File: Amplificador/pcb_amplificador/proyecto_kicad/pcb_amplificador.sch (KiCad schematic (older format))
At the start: 139 parts, among them CON1 SJ-3523-SMT-TR, J1 Screw_Terminal_01x02, J2 Screw_Terminal_01x02, J3 Screw_Terminal_01x02, J4 Screw_Terminal_01x02, J5 Conn_01x03_Male, J6 Screw_Terminal_01x02, J7 Screw_Terminal_01x02, K1 FINDER-40.11-2016, M1 FDS9934C, M2 FDS9934C, Q1 BC860, Q10 BD139, Q11 BD140, Q12 BD139, Q13 2SA1943-O_Q_, Q14 2SC5200-O_Q, Q15 2SA1943-O_Q_, Q16 2SC5200-O_Q, Q17 2SAR514P5, Q18 BC860, Q19 BC860, Q2 BC860, Q20 2SAR514P5, Q21 2SCR514P5, Q22 2SCR514P5, Q23 2SCR514P5, Q24 2SAR514P5, Q25 2SCR514P5, Q26 BC817, Q27 BC817, Q28 BC807, Q29 BS170, Q3 BC850, Q4 BC850, Q5 BC860, Q6 BC860, Q7 BC850, Q8 2SCR514P5, Q9 2SCR514P5

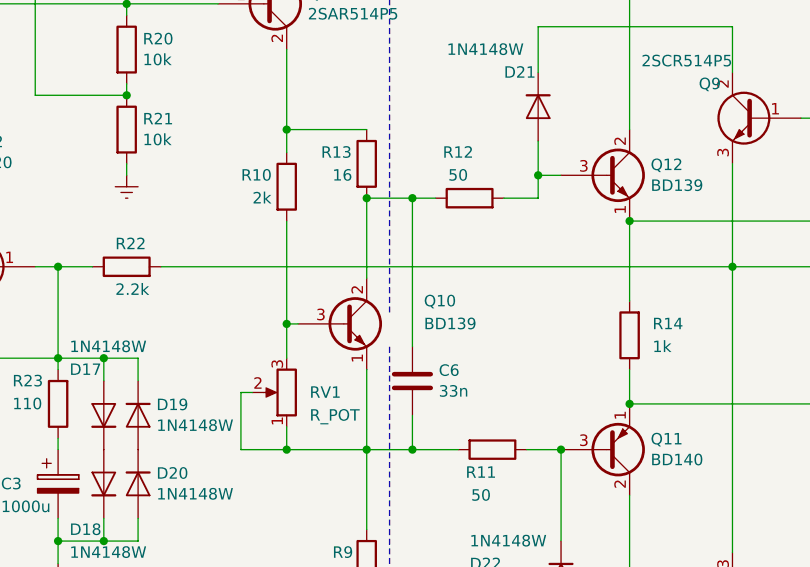
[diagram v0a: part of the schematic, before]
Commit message: Cambios varios en la documentación del amplificador; agregado de ecuaciones en latex y gráficos al archivo que explica como se hallaron los valores de los componentes; agregado de documento que explica paso a paso el funcionamiento de los conmutadores de salida
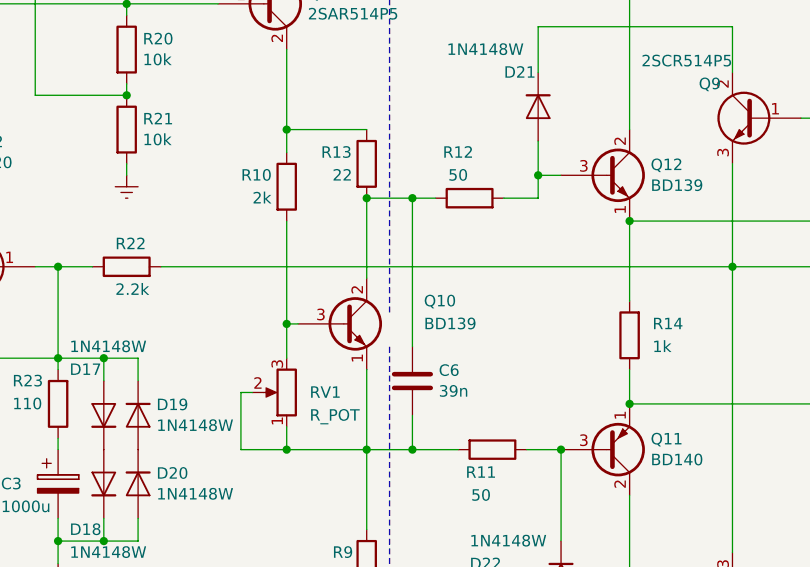
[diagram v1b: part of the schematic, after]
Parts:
- C6: value 33n -> 39n
- R13: value 16 -> 22
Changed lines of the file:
@@
 EESchema Schematic File Version 4
 LIBS:pcb_amplificador-cache
-EELAYER 26 0
+EELAYER 29 0
 EELAYER END
 $Descr A4 11693 8268
@@
 P 4150 2700
 F 0 "R13" H 3950 2750 50  0000 L CNN
-F 1 "16" H 4000 2650 50  0000 L CNN
+F 1 "22" H 4000 2650 50  0000 L CNN
 F 2 "Resistor_SMD:R_0805_2012Metric_Pad1.15x1.40mm_HandSolder" V 4080 2700 50  0001 C CNN
 F 3 "~" H 4150 2700 50  0001 C CNN
@@
 P 4350 3650
 F 0 "C6" H 4235 3604 50  0000 R CNN
-F 1 "33n" H 4235 3695 50  0000 R CNN
+F 1 "39n" H 4235 3695 50  0000 R CNN
 F 2 "Capacitor_SMD:C_0805_2012Metric_Pad1.15x1.40mm_HandSolder" H 4388 3500 50  0001 C CNN
 F 3 "~" H 4350 3650 50  0001 C CNN

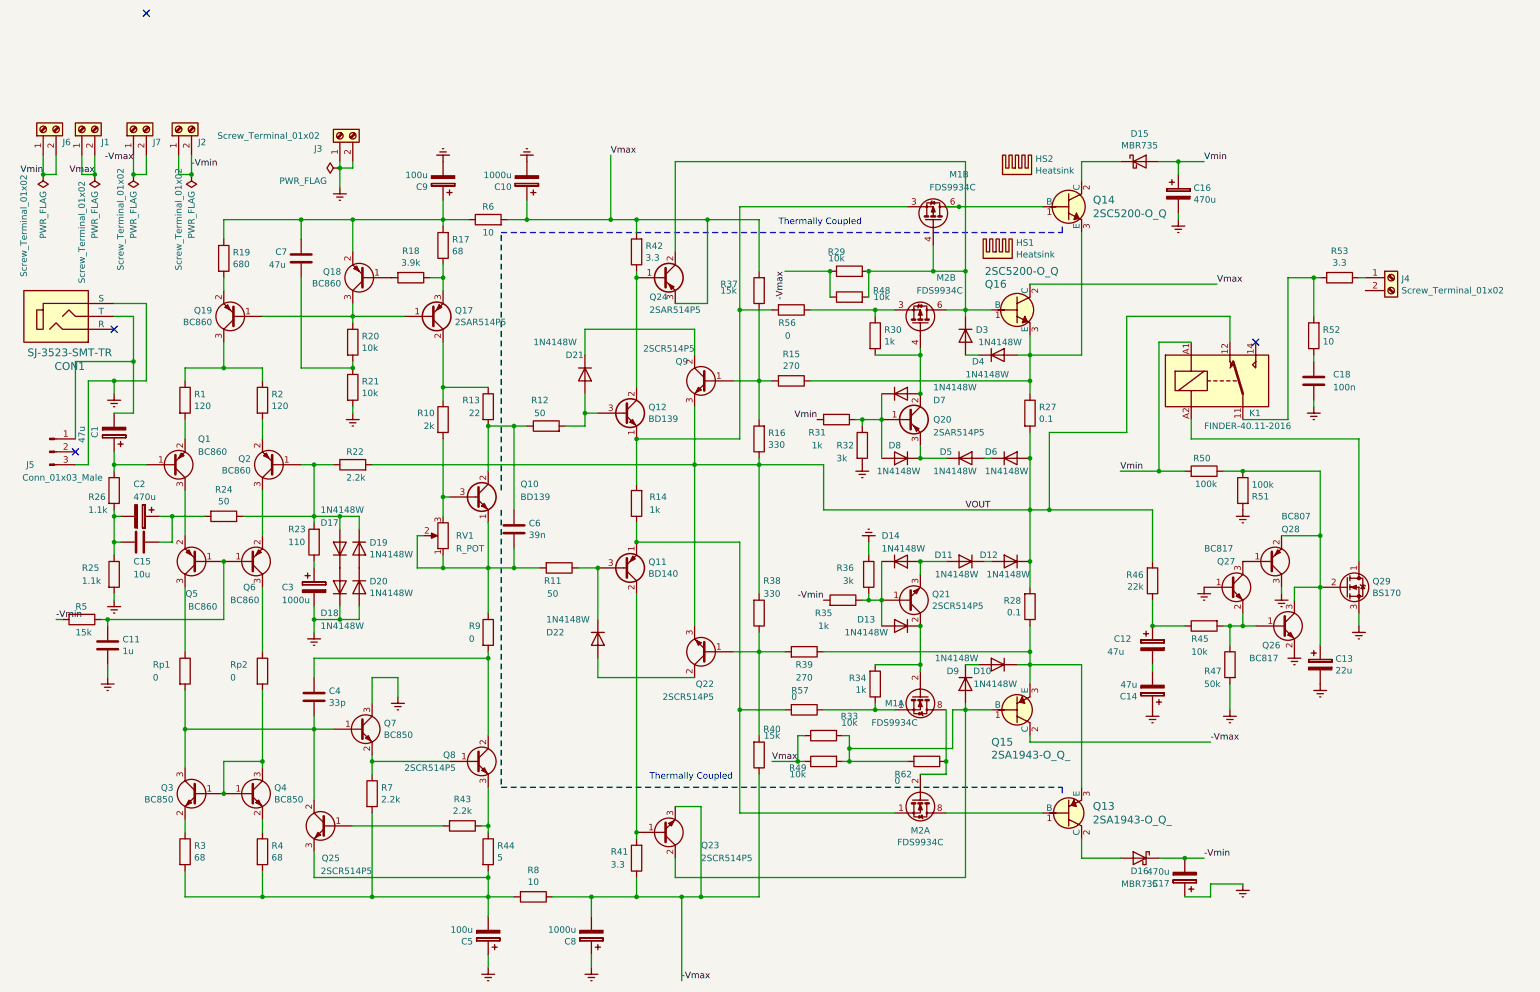
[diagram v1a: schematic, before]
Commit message: Agregado de datos extra de los componentes en el esquemático del amplificador y cambios menores
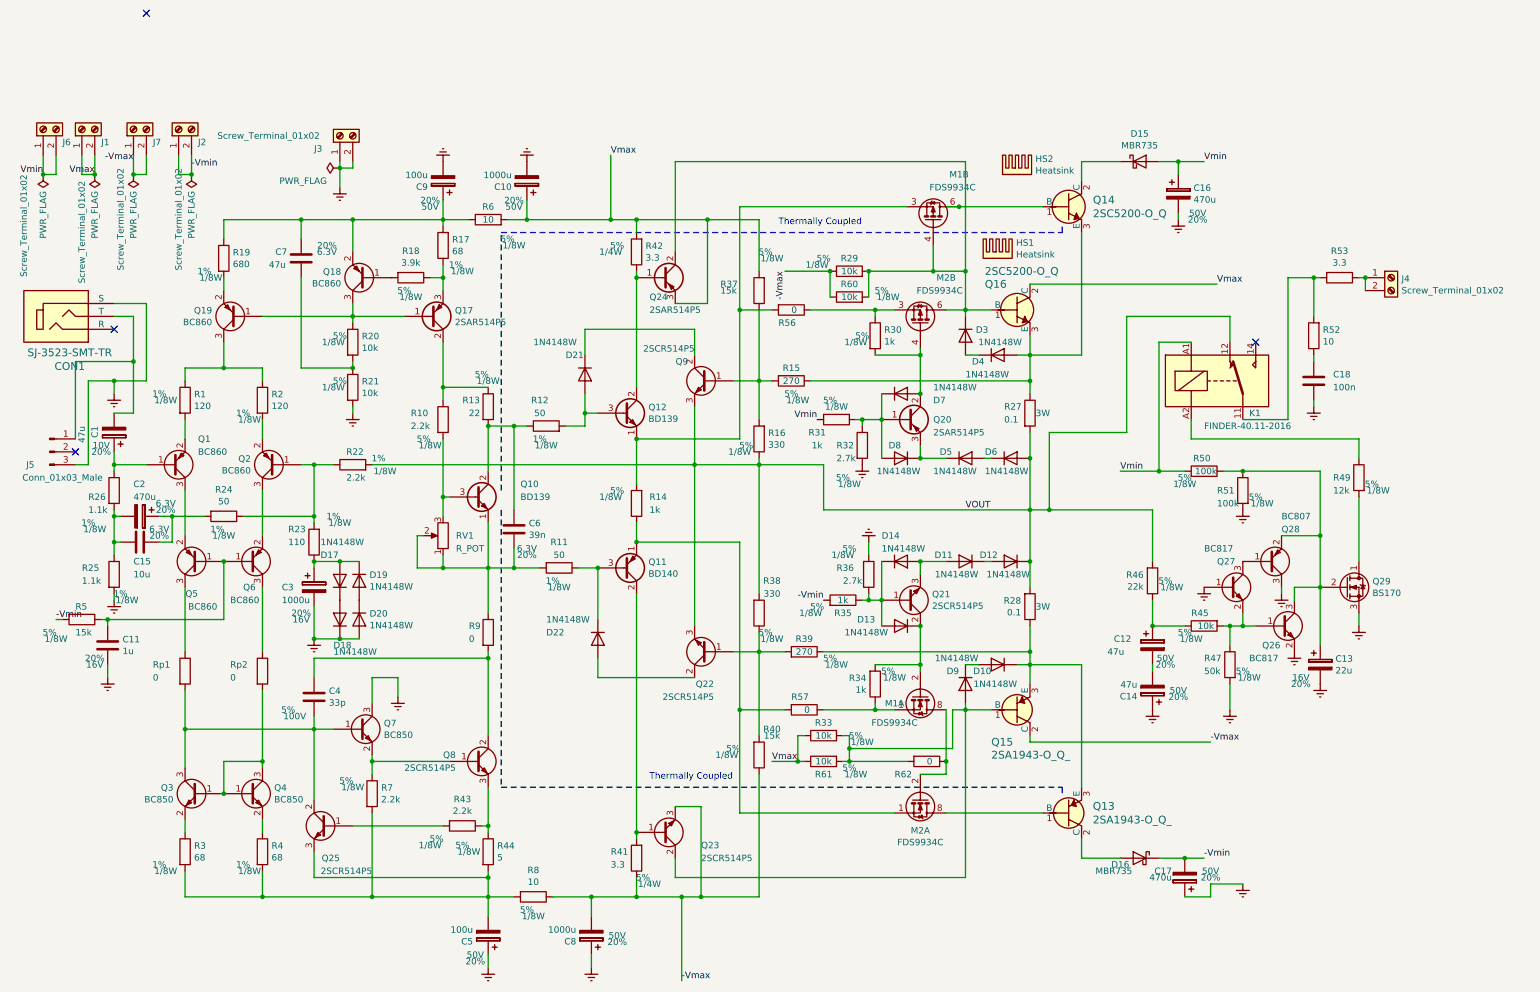
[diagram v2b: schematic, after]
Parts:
- added R49: 12k, Resistor_SMD:R_0805_2012Metric_Pad1.15x1.40mm_HandSolder, symbol Device:R
- C1: Tolerance (none) -> 20%; Voltage (none) -> 10V
- C10, C12, C14, C16, C17, C5, C8, C9: Tolerance (none) -> 20%; Voltage (none) -> 50V
- C11, C13, C3: Tolerance (none) -> 20%; Voltage (none) -> 16V
- C15, C2, C6, C7: Tolerance (none) -> 20%; Voltage (none) -> 6.3V
- C4: Tolerance (none) -> 5%; Voltage (none) -> 100V
- R1, R11, R12, R17, R19, R2, R22, R23, R24, R25, R26, R3, R4: Power (none) -> 1/8W; Tolerance (none) -> 1%
- R10: value 2k -> 2.2k; Power (none) -> 1/8W; Tolerance (none) -> 5%
- R13, R14, R15, R16, R18, R20, R21, R29, R30, R31, R33, R34, R35, R37, R38, R39, R40, R43, R44, R45, R46, R47, R5, R50, R51, R6, R7, R8: Power (none) -> 1/8W; Tolerance (none) -> 5%
- R27, R28: Power (none) -> 3W
- R32, R36: value 3k -> 2.7k; Power (none) -> 1/8W; Tolerance (none) -> 5%
- R41, R42: Power (none) -> 1/4W; Tolerance (none) -> 5%
- R60: renamed from R48; Power (none) -> 1/8W; Tolerance (none) -> 5%
- R61: renamed from R49; Power (none) -> 1/8W; Tolerance (none) -> 5%
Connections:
- net at Q2.1 (B), R22.1, R23.2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: no longer D17.2 (A), D19.1 (K)
- net at C3.1, R23.1: now also D17.2 (A), D19.1 (K)
- net at J4.1 (Pin_1), R53.1: now also J4.2 (Pin_2)
- net at Q29.1 (D): now also R49.2; no longer K1.A2
- new net: K1.A2, R49.1
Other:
- moved on the sheet: D17, D18, D19, D20

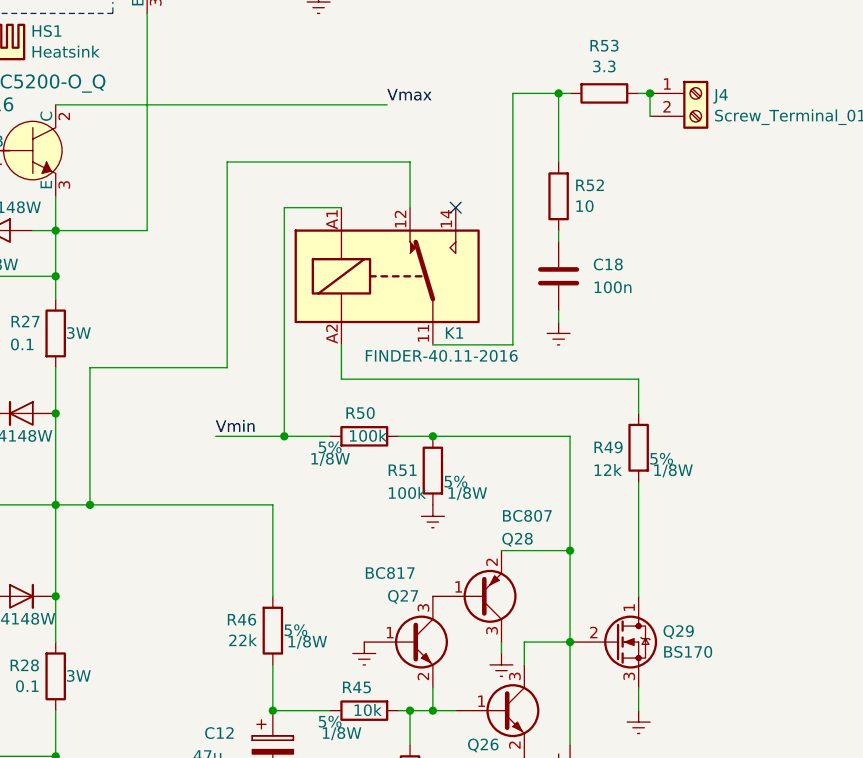
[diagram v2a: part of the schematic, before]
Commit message: Agregado de los resultados de la medicion de la proteccion de DC
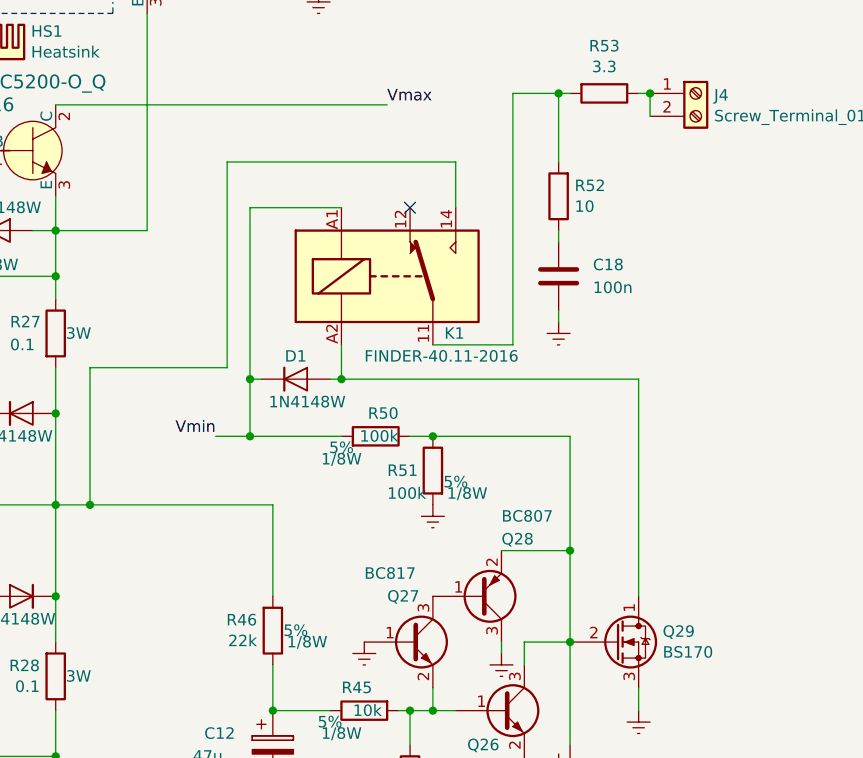
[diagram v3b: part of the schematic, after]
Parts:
- removed R49: 12k, Resistor_SMD:R_0805_2012Metric_Pad1.15x1.40mm_HandSolder, symbol Device:R
- added D1: 1N4148W, Diode_SMD:D_SOD-123, symbol Diode:1N4148W
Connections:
- net VOUT: now also K1.14; no longer K1.12
- net Vmin: now also D1.1 (K)
- net at Q29.1 (D): now also K1.A2, D1.2 (A)
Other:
- moved on the sheet: R50
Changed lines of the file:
@@
 EESchema Schematic File Version 4
 LIBS:pcb_amplificador-cache
-EELAYER 26 0
+EELAYER 29 0
 EELAYER END
 $Descr A4 11693 8268
@@
 L Device:R R50
 U 1 1 5D0A4886
-P 9700 3200
-F 0 "R50" V 9800 3250 50  0000 R CNN
-F 1 "100k" V 9700 3300 50  0000 R CNN
-F 2 "Resistor_SMD:R_0805_2012Metric_Pad1.15x1.40mm_HandSolder" V 9630 3200 50  0001 C CNN
-F 3 "~" H 9700 3200 50  0001 C CNN
-F 4 "5%" V 9650 3050 50  0000 C CNN "Tolerance"
-F 5 "1/8W" V 9600 3050 50  0000 C CNN "Power"
-	1    9700 3200
+P 9750 3200
+F 0 "R50" V 9850 3300 50  0000 R CNN
+F 1 "100k" V 9750 3300 50  0000 R CNN
+F 2 "Resistor_SMD:R_0805_2012Metric_Pad1.15x1.40mm_HandSolder" V 9680 3200 50  0001 C CNN
+F 3 "~" H 9750 3200 50  0001 C CNN
+F 4 "5%" V 9700 3050 50  0000 C CNN "Tolerance"
+F 5 "1/8W" V 9650 3050 50  0000 C CNN "Power"
+	1    9750 3200
 	0    1    -1   0
 $EndComp
@@
 $EndComp
 Wire Wire Line
-	9850 3200 10000 3200
+	9900 3200 10000 3200
 Wire Wire Line
 	10600 3200 10600 3700
@@
 	10600 4100 10600 4550
 Wire Wire Line
-	10900 3900 10900 3400
-Wire Wire Line
-	9350 3200 9350 2200
-Wire Wire Line
 	9100 2000 9100 2900
 Wire Wire Line
@@
 Wire Wire Line
 	10600 3700 10600 4100
-Wire Wire Line
-	9350 3200 9550 3200
 Wire Wire Line
 	10000 3200 10600 3200
@@
 Text Label 9750 5300 0    50   ~ 0
 -Vmax
-Text Label 9050 3200 0    50   ~ 0
+Text Label 9050 3200 2    50   ~ 0
 Vmin
 Text Label 9800 1750 0    50   ~ 0
@@
 Wire Wire Line
 	4150 4650 4150 5250
-Wire Wire Line
-	9350 2200 9600 2200
 Text Label 7850 3500 0    50   ~ 0
 VOUT
@@
 Text Label 6750 4200 2    50   ~ 0
 -Vmin
-Connection ~ 9350 3200
 Connection ~ 6800 1650
 $Comp
@@
 	-1   0    0    1
 $EndComp
-Wire Wire Line
-	9050 3200 9350 3200
-Wire Wire Line
-	9900 2200 9900 2000
-Wire Wire Line
-	9900 2000 9100 2000
-NoConn ~ 10100 2200
 $Comp
 L Transistor_BJT:BD139 Q10
@@
 	1750 900  1850 900
 Connection ~ 1850 900
-$Comp
-L Relay:FINDER-40.11-2016 K1
-U 1 1 5DA9AF8C
-P 9800 2500
-F 0 "K1" H 10050 2250 50  0000 L CNN
-F 1 "FINDER-40.11-2016" H 9700 2150 50  0000 L CNN
-F 2 "Relay_THT:Relay_SPDT_Schrack-RP-II-1-16A-FormC_RM5mm" H 10940 2460 50  0001 C CNN
-F 3 "https://www.finder-relais.net/de/finder-relais-serie-40.pdf" H 9800 2500 50  0001 C CNN
-	1    9800 2500
-	1    0    0    -1
-$EndComp
-Wire Wire Line
-	9600 2950 9600 2800
 Wire Wire Line
 	9600 2950 10900 2950
@@
 Connection ~ 10950 1700
 Connection ~ 4150 2850
-$Comp
-L Device:R R49
-U 1 1 5D7228B4
-P 10900 3250
-F 0 "R49" H 11100 3250 50  0000 R CNN
-F 1 "12k" H 11100 3150 50  0000 R CNN
-F 2 "Resistor_SMD:R_0805_2012Metric_Pad1.15x1.40mm_HandSolder" V 10830 3250 50  0001 C CNN
-F 3 "~" H 10900 3250 50  0001 C CNN
-F 4 "5%" H 10800 3200 50  0000 C CNN "Tolerance"
-F 5 "1/8W" H 10750 3150 50  0000 C CNN "Power"
-	1    10900 3250
-	-1   0    0    -1
-$EndComp
-Wire Wire Line
-	10900 3100 10900 2950
+Wire Wire Line
+	10900 2950 10900 3900
+$Comp
+L Diode:1N4148W D1
+U 1 1 5D6AF4C4
+P 9400 2950
+F 0 "D1" H 9400 3050 50  0000 C CNN
+F 1 "1N4148W" H 9450 2850 50  0000 C CNN
+F 2 "Diode_SMD:D_SOD-123" H 9400 2775 50  0001 C CNN
+F 3 "https://www.vishay.com/docs/85748/1n4148w.pdf" H 9400 2950 50  0001 C CNN
+	1    9400 2950
+	1    0    0    -1
+$EndComp
+Wire Wire Line
+	9600 2800 9600 2950
+Connection ~ 9600 2950
+Wire Wire Line
+	9050 3200 9200 3200
+Wire Wire Line
+	9600 2950 9550 2950
+Wire Wire Line
+	9250 2950 9200 2950
+Wire Wire Line
+	9200 2950 9200 3200
+Connection ~ 9200 3200
+Wire Wire Line
+	9200 3200 9600 3200
+Wire Wire Line
+	9200 2950 9200 2200
+Wire Wire Line
+	9200 2200 9600 2200
+Connection ~ 9200 2950
+$Comp
+L Relay:FINDER-40.11-2016 K1
+U 1 1 5DA9AF8C
+P 9800 2500
+F 0 "K1" H 10050 2250 50  0000 L CNN
+F 1 "FINDER-40.11-2016" H 9700 2150 50  0000 L CNN
+F 2 "Relay_THT:Relay_SPDT_Schrack-RP-II-1-16A-FormC_RM5mm" H 10940 2460 50  0001 C CNN
+F 3 "https://www.finder-relais.net/de/finder-relais-serie-40.pdf" H 9800 2500 50  0001 C CNN
+	1    9800 2500
+	1    0    0    -1
+$EndComp
+Wire Wire Line
+	10100 2000 10100 2200
+Wire Wire Line
+	9100 2000 10100 2000
+NoConn ~ 9900 2200
 $EndSCHEMATC

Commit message: Agregado de los resultados de las mediciones de THD con las protecciones y desarrollo de la explicación del comportamiento de los limitadores de corriente en el semicilo negativo
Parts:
- R37, R40: value 15k -> 11k
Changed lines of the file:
@@
 EESchema Schematic File Version 4
 LIBS:pcb_amplificador-cache
-EELAYER 29 0
+EELAYER 26 0
 EELAYER END
 $Descr A4 11693 8268
@@
 P 6250 5400
 F 0 "R40" H 6350 5200 50  0000 C CNN
-F 1 "15k" H 6350 5250 50  0000 C CNN
+F 1 "11k" H 6350 5250 50  0000 C CNN
 F 2 "Resistor_SMD:R_0805_2012Metric_Pad1.15x1.40mm_HandSolder" V 6180 5400 50  0001 C CNN
 F 3 "~" H 6250 5400 50  0001 C CNN
@@
 P 6250 1800
 F 0 "R37" H 6550 1750 50  0000 R CNN
-F 1 "15k" H 6550 1800 50  0000 R CNN
+F 1 "11k" H 6550 1800 50  0000 R CNN
 F 2 "Resistor_SMD:R_0805_2012Metric_Pad1.15x1.40mm_HandSolder" V 6180 1800 50  0001 C CNN
 F 3 "~" H 6250 1800 50  0001 C CNN
